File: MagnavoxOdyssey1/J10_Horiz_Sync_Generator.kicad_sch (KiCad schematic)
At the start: 15 parts

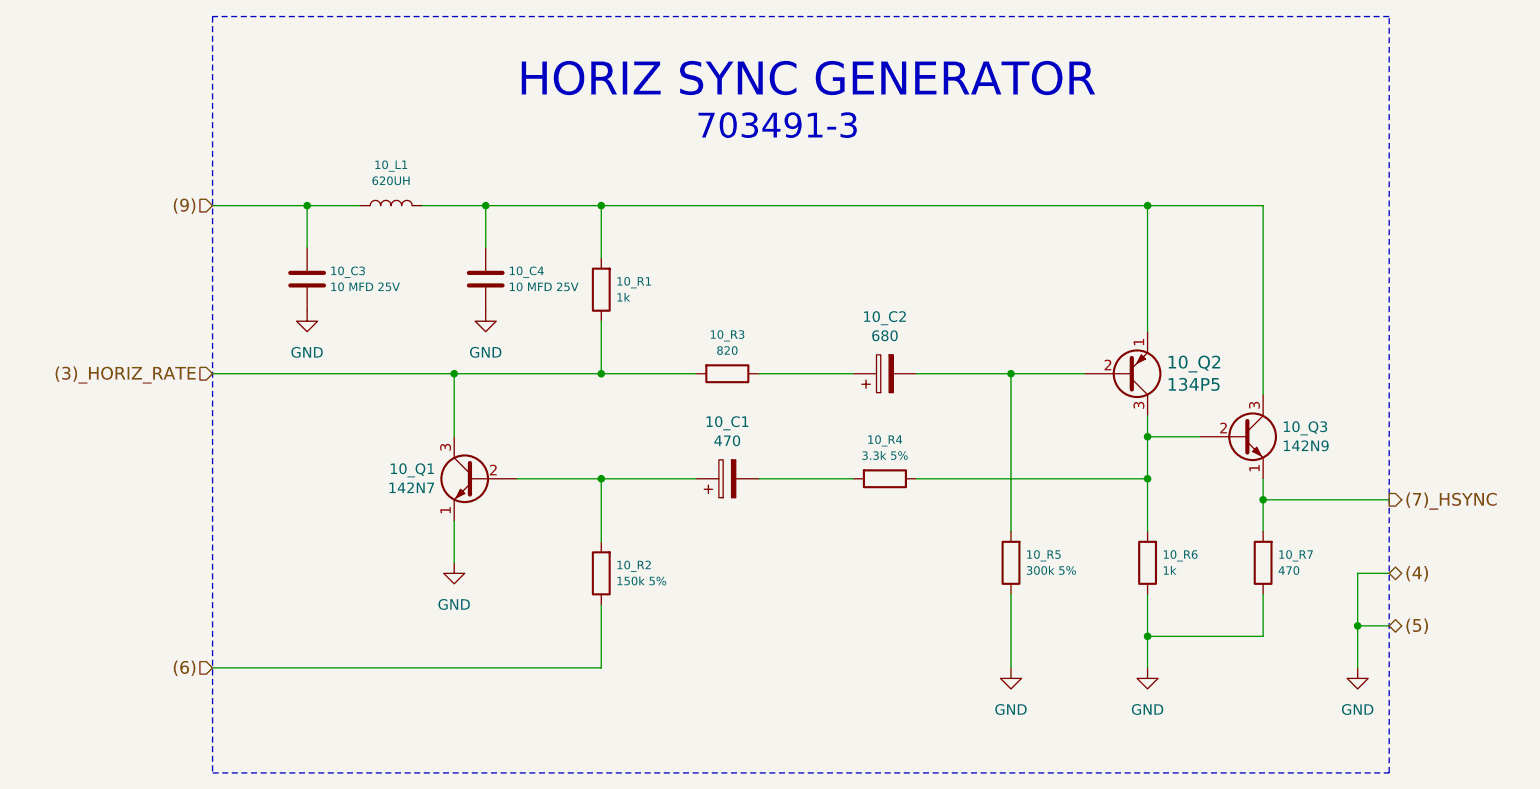
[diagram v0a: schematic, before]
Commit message: update to kicad 9
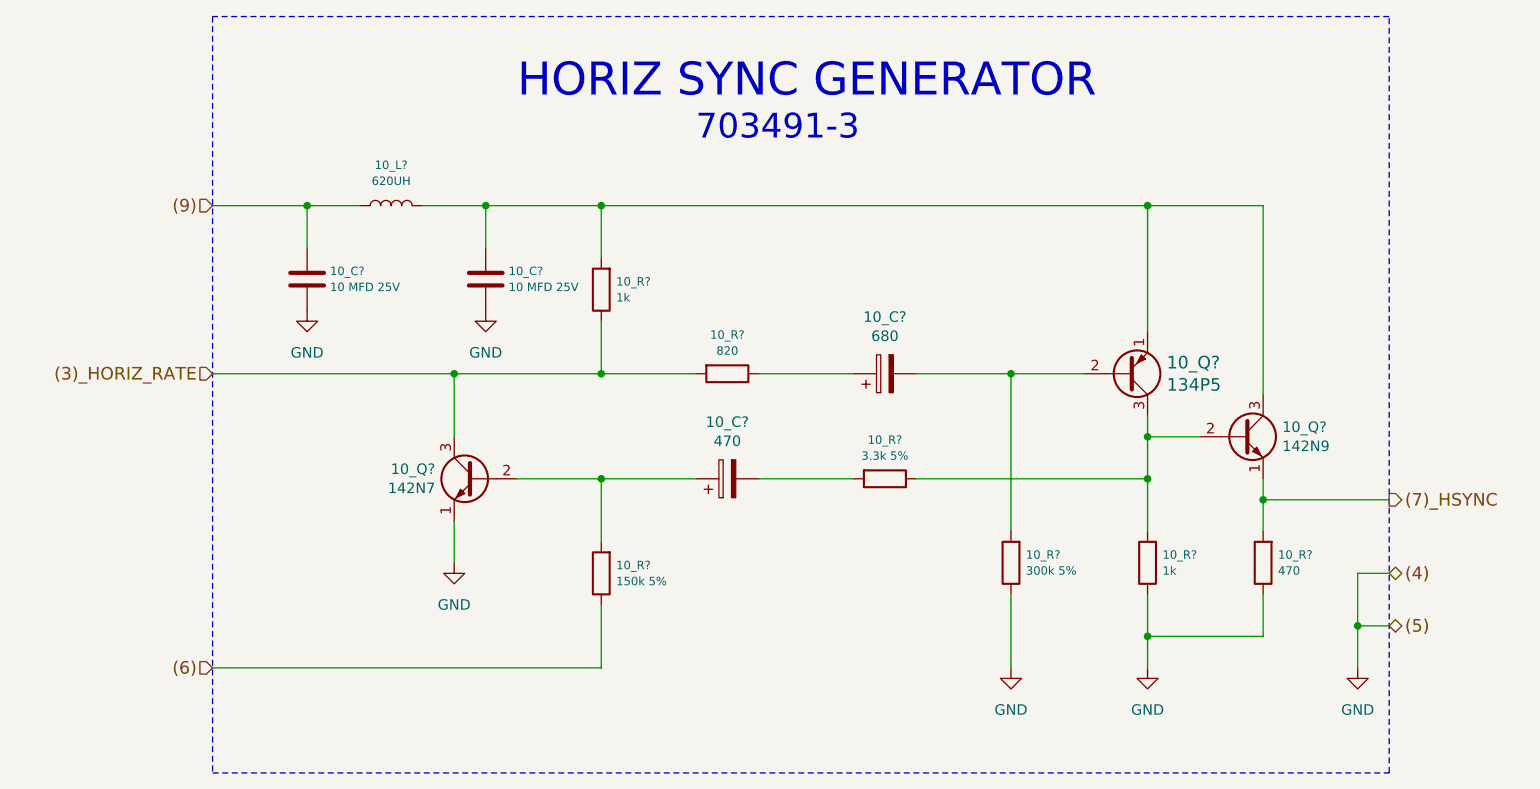
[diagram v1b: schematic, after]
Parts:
- 10_Q?: renamed from 10_Q1; symbol Device:Q_NPN_EBC -> Transistor_BJT:Q_NPN_EBC
- 10_Q?: renamed from 10_Q2; symbol Device:Q_PNP_EBC -> Transistor_BJT:Q_PNP_EBC
- 10_Q?: renamed from 10_Q3; symbol Device:Q_NPN_EBC -> Transistor_BJT:Q_NPN_EBC
- renumbered 10_C3 to 10_C?, 10_C4 to 10_C?, 10_C1 to 10_C?, 10_C2 to 10_C?, 10_L1 to 10_L?, 10_R1 to 10_R?, 10_R5 to 10_R?, 10_R6 to 10_R?, 10_R2 to 10_R?, 10_R7 to 10_R?, 10_R4 to 10_R?, 10_R3 to 10_R?
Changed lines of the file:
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@@
 (kicad_sch
-	(version 20231120)
+	(version 20250114)
 	(generator "eeschema")
-	(generator_version "8.0")
+	(generator_version "9.0")
 	(paper "A4")
+	(text "HORIZ SYNC GENERATOR"
+		(exclude_from_sim no)
+		(at 113.03 63.5 0)
+		(effects
+			(font
+				(size 3.9878 3.9878)
+			)
+			(justify left bottom)
+		)
+	)
+	(text "703491-3"
+		(exclude_from_sim no)
+		(at 134.62 68.58 0)
+		(effects
+			(font
+				(size 2.9972 2.9972)
+			)
+			(justify left bottom)
+		)
+	)
 	(junction
 		(at 123.19 76.2)
@@
 			(width 0)
 			(type default)
-		)
-	)
-	(text "HORIZ SYNC GENERATOR"
-		(exclude_from_sim no)
-		(at 113.03 63.5 0)
-		(effects
-			(font
-				(size 3.9878 3.9878)
-			)
-			(justify left bottom)
-		)
-	)
-	(text "703491-3"
-		(exclude_from_sim no)
-		(at 134.62 68.58 0)
-		(effects
-			(font
-				(size 2.9972 2.9972)
-			)
-			(justify left bottom)
 		)
 	)
@@
 		(on_board yes)
 		(dnp no)
-		(property "Reference" "10_C3"
+		(property "Reference" "10_C?"
 			(at 90.3986 84.1248 0)
 			(effects
@@
 		)
 		(pin "2"
+		)
+		(instances
+			(project "MagnavoxOdyssey1"
+				(path "/adb6e295-eae5-402e-a614-02a705c3e27c/00000000-0000-0000-0000-0000588f18cd"
+					(reference "10_C?")
+					(unit 1)
+				)
+			)
 		)
 	)
@@
 		(on_board yes)
 		(dnp no)
-		(property "Reference" "10_C4"
+		(property "Reference" "10_C?"
 			(at 111.9886 84.1248 0)
 			(effects
@@
 		)
 		(pin "2"
+		)
+		(instances
+			(project "MagnavoxOdyssey1"
+				(path "/adb6e295-eae5-402e-a614-02a705c3e27c/00000000-0000-0000-0000-0000588f18cd"
+					(reference "10_C?")
+					(unit 1)
+				)
+			)
 		)
 	)
@@
 		(on_board yes)
 		(dnp no)
-		(property "Reference" "10_L1"
+		(property "Reference" "10_L?"
 			(at 97.79 71.2978 90)
 			(effects
@@
 		)
 		(pin "2"
+		)
+		(instances
+			(project "MagnavoxOdyssey1"
+				(path "/adb6e295-eae5-402e-a614-02a705c3e27c/00000000-0000-0000-0000-0000588f18cd"
+					(reference "10_L?")
+					(unit 1)
+				)
+			)
 		)
 	)
@@
 		(on_board yes)
 		(dnp no)
-		(property "Reference" "10_R1"
+		(property "Reference" "10_R?"
 			(at 124.9934 85.3948 0)
 			(effects
@@
 		)
 		(pin "2"
+		)
+		(instances
+			(project "MagnavoxOdyssey1"
+				(path "/adb6e295-eae5-402e-a614-02a705c3e27c/00000000-0000-0000-0000-0000588f18cd"
+					(reference "10_R?")
+					(unit 1)
+				)
+			)
 		)
 	)
@@
 		(on_board yes)
 		(dnp no)
-		(property "Reference" "10_R5"
+		(property "Reference" "10_R?"
 			(at 174.5234 118.4148 0)
 			(effects
@@
 		)
 		(pin "2"
+		)
+		(instances
+			(project "MagnavoxOdyssey1"
+				(path "/adb6e295-eae5-402e-a614-02a705c3e27c/00000000-0000-0000-0000-0000588f18cd"
+					(reference "10_R?")
+					(unit 1)
+				)
+			)
 		)
 	)
@@
 		(on_board yes)
 		(dnp no)
-		(property "Reference" "10_R6"
+		(property "Reference" "10_R?"
 			(at 191.0334 118.4148 0)
 			(effects
@@
 		(pin "2"
 		)
+		(instances
+			(project "MagnavoxOdyssey1"
+				(path "/adb6e295-eae5-402e-a614-02a705c3e27c/00000000-0000-0000-0000-0000588f18cd"
+					(reference "10_R?")
+					(unit 1)
+				)
+			)
+		)
 	)
 	(symbol
-		(lib_id "Device:Q_NPN_EBC")
+		(lib_id "Transistor_BJT:Q_NPN_EBC")
 		(at 107.95 109.22 0)
 		(mirror y)
@@
 		(on_board yes)
 		(dnp no)
-		(property "Reference" "10_Q1"
+		(property "Reference" "10_Q?"
 			(at 103.124 108.0516 0)
 			(effects
@@
 		)
 		(pin "3"
+		)
+		(instances
+			(project "MagnavoxOdyssey1"
+				(path "/adb6e295-eae5-402e-a614-02a705c3e27c/00000000-0000-0000-0000-0000588f18cd"
+					(reference "10_Q?")
+					(unit 1)
+				)
+			)
 		)
 	)
@@
 		(on_board yes)
 		(dnp no)
-		(property "Reference" "10_R2"
+		(property "Reference" "10_R?"
 			(at 124.9934 119.6848 0)
 			(effects
@@
 		)
 		(pin "2"
+		)
+		(instances
+			(project "MagnavoxOdyssey1"
+				(path "/adb6e295-eae5-402e-a614-02a705c3e27c/00000000-0000-0000-0000-0000588f18cd"
+					(reference "10_R?")
+					(unit 1)
+				)
+			)
 		)
 	)
@@
 	)
 	(symbol
-		(lib_id "Device:Q_PNP_EBC")
+		(lib_id "Transistor_BJT:Q_PNP_EBC")
 		(at 186.69 96.52 0)
 		(mirror x)
@@
 		(on_board yes)
 		(dnp no)
-		(property "Reference" "10_Q2"
+		(property "Reference" "10_Q?"
 			(at 191.5414 95.1738 0)
 			(effects
@@
 		)
 		(pin "3"
+		)
+		(instances
+			(project "MagnavoxOdyssey1"
+				(path "/adb6e295-eae5-402e-a614-02a705c3e27c/00000000-0000-0000-0000-0000588f18cd"
+					(reference "10_Q?")
+					(unit 1)
+				)
+			)
 		)
 	)
@@
 	)
 	(symbol
-		(lib_id "Device:Q_NPN_EBC")
+		(lib_id "Transistor_BJT:Q_NPN_EBC")
 		(at 200.66 104.14 0)
 		(unit 1)
@@
 		(on_board yes)
 		(dnp no)
-		(property "Reference" "10_Q3"
+		(property "Reference" "10_Q?"
 			(at 205.5114 102.9716 0)
 			(effects
@@
 		)
 		(pin "3"
+		)
+		(instances
+			(project "MagnavoxOdyssey1"
+				(path "/adb6e295-eae5-402e-a614-02a705c3e27c/00000000-0000-0000-0000-0000588f18cd"
+					(reference "10_Q?")
+					(unit 1)
+				)
+			)
 		)
 	)
@@
 		(on_board yes)
 		(dnp no)
-		(property "Reference" "10_R7"
+		(property "Reference" "10_R?"
 			(at 205.0034 118.4148 0)
 			(effects
@@
 		)
 		(pin "2"
+		)
+		(instances
+			(project "MagnavoxOdyssey1"
+				(path "/adb6e295-eae5-402e-a614-02a705c3e27c/00000000-0000-0000-0000-0000588f18cd"
+					(reference "10_R?")
+					(unit 1)
+				)
+			)
 		)
 	)
@@
 		(on_board yes)
 		(dnp no)
-		(property "Reference" "10_R4"
+		(property "Reference" "10_R?"
 			(at 157.48 104.521 90)
 			(effects
@@
 		)
 		(pin "2"
+		)
+		(instances
+			(project "MagnavoxOdyssey1"
+				(path "/adb6e295-eae5-402e-a614-02a705c3e27c/00000000-0000-0000-0000-0000588f18cd"
+					(reference "10_R?")
+					(unit 1)
+				)
+			)
 		)
 	)
@@
 		(on_board yes)
 		(dnp no)
-		(property "Reference" "10_C1"
+		(property "Reference" "10_C?"
 			(at 138.43 102.362 90)
 			(effects
@@
 		)
 		(pin "2"
+		)
+		(instances
+			(project "MagnavoxOdyssey1"
+				(path "/adb6e295-eae5-402e-a614-02a705c3e27c/00000000-0000-0000-0000-0000588f18cd"
+					(reference "10_C?")
+					(unit 1)
+				)
+			)
 		)
 	)
@@
 		(on_board yes)
 		(dnp no)
-		(property "Reference" "10_C2"
+		(property "Reference" "10_C?"
 			(at 157.48 89.662 90)
 			(effects
@@
 		)
 		(pin "2"
+		)
+		(instances
+			(project "MagnavoxOdyssey1"
+				(path "/adb6e295-eae5-402e-a614-02a705c3e27c/00000000-0000-0000-0000-0000588f18cd"
+					(reference "10_C?")
+					(unit 1)
+				)
+			)
 		)
 	)
@@
 		(on_board yes)
 		(dnp no)
-		(property "Reference" "10_R3"
+		(property "Reference" "10_R?"
 			(at 138.43 91.821 90)
 			(effects
@@
 		(pin "2"
 		)
-	)
+		(instances
+			(project "MagnavoxOdyssey1"
+				(path "/adb6e295-eae5-402e-a614-02a705c3e27c/00000000-0000-0000-0000-0000588f18cd"
+					(reference "10_R?")
+					(unit 1)
+				)
+			)
+		)
+	)

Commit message: annotate
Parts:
- gave numbers to parts that had none: 15
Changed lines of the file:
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@@
 		(on_board yes)
 		(dnp no)
-		(property "Reference" "10_C?"
+		(property "Reference" "10_C1"
 			(at 90.3986 84.1248 0)
 			(effects
@@
 			(project "MagnavoxOdyssey1"
 				(path "/adb6e295-eae5-402e-a614-02a705c3e27c/00000000-0000-0000-0000-0000588f18cd"
-					(reference "10_C?")
+					(reference "10_C1")
 					(unit 1)
 				)
@@
 		(on_board yes)
 		(dnp no)
-		(property "Reference" "10_C?"
+		(property "Reference" "10_C2"
 			(at 111.9886 84.1248 0)
 			(effects
@@
 			(project "MagnavoxOdyssey1"
 				(path "/adb6e295-eae5-402e-a614-02a705c3e27c/00000000-0000-0000-0000-0000588f18cd"
-					(reference "10_C?")
+					(reference "10_C2")
 					(unit 1)
 				)
@@
 		(on_board yes)
 		(dnp no)
-		(property "Reference" "10_L?"
+		(property "Reference" "10_L1"
 			(at 97.79 71.2978 90)
 			(effects
@@
 			(project "MagnavoxOdyssey1"
 				(path "/adb6e295-eae5-402e-a614-02a705c3e27c/00000000-0000-0000-0000-0000588f18cd"
-					(reference "10_L?")
+					(reference "10_L1")
 					(unit 1)
 				)
@@
 		(on_board yes)
 		(dnp no)
-		(property "Reference" "10_R?"
+		(property "Reference" "10_R1"
 			(at 124.9934 85.3948 0)
 			(effects
@@
 			(project "MagnavoxOdyssey1"
 				(path "/adb6e295-eae5-402e-a614-02a705c3e27c/00000000-0000-0000-0000-0000588f18cd"
-					(reference "10_R?")
+					(reference "10_R1")
 					(unit 1)
 				)
@@
 		(on_board yes)
 		(dnp no)
-		(property "Reference" "10_R?"
+		(property "Reference" "10_R4"
 			(at 174.5234 118.4148 0)
 			(effects
@@
 			(project "MagnavoxOdyssey1"
 				(path "/adb6e295-eae5-402e-a614-02a705c3e27c/00000000-0000-0000-0000-0000588f18cd"
-					(reference "10_R?")
+					(reference "10_R4")
 					(unit 1)
 				)
@@
 		(on_board yes)
 		(dnp no)
-		(property "Reference" "10_R?"
+		(property "Reference" "10_R5"
 			(at 191.0334 118.4148 0)
 			(effects
@@
 			(project "MagnavoxOdyssey1"
 				(path "/adb6e295-eae5-402e-a614-02a705c3e27c/00000000-0000-0000-0000-0000588f18cd"
-					(reference "10_R?")
+					(reference "10_R5")
 					(unit 1)
 				)
@@
 		(on_board yes)
 		(dnp no)
-		(property "Reference" "10_Q?"
+		(property "Reference" "10_Q3"
 			(at 103.124 108.0516 0)
 			(effects
@@
 			(project "MagnavoxOdyssey1"
 				(path "/adb6e295-eae5-402e-a614-02a705c3e27c/00000000-0000-0000-0000-0000588f18cd"
-					(reference "10_Q?")
+					(reference "10_Q3")
 					(unit 1)
 				)
@@
 		(on_board yes)
 		(dnp no)
-		(property "Reference" "10_R?"
+		(property "Reference" "10_R7"
 			(at 124.9934 119.6848 0)
 			(effects
@@
 			(project "MagnavoxOdyssey1"
 				(path "/adb6e295-eae5-402e-a614-02a705c3e27c/00000000-0000-0000-0000-0000588f18cd"
-					(reference "10_R?")
+					(reference "10_R7")
 					(unit 1)
 				)
@@
 		(on_board yes)
 		(dnp no)
-		(property "Reference" "10_Q?"
+		(property "Reference" "10_Q1"
 			(at 191.5414 95.1738 0)
 			(effects
@@
 			(project "MagnavoxOdyssey1"
 				(path "/adb6e295-eae5-402e-a614-02a705c3e27c/00000000-0000-0000-0000-0000588f18cd"
-					(reference "10_Q?")
+					(reference "10_Q1")
 					(unit 1)
 				)
@@
 		(on_board yes)
 		(dnp no)
-		(property "Reference" "10_Q?"
+		(property "Reference" "10_Q2"
 			(at 205.5114 102.9716 0)
 			(effects
@@
 			(project "MagnavoxOdyssey1"
 				(path "/adb6e295-eae5-402e-a614-02a705c3e27c/00000000-0000-0000-0000-0000588f18cd"
-					(reference "10_Q?")
+					(reference "10_Q2")
 					(unit 1)
 				)
@@
 		(on_board yes)
 		(dnp no)
-		(property "Reference" "10_R?"
+		(property "Reference" "10_R6"
 			(at 205.0034 118.4148 0)
 			(effects
@@
 			(project "MagnavoxOdyssey1"
 				(path "/adb6e295-eae5-402e-a614-02a705c3e27c/00000000-0000-0000-0000-0000588f18cd"
-					(reference "10_R?")
+					(reference "10_R6")
 					(unit 1)
 				)
@@
 		(on_board yes)
 		(dnp no)
-		(property "Reference" "10_R?"
+		(property "Reference" "10_R3"
 			(at 157.48 104.521 90)
 			(effects
@@
 			(project "MagnavoxOdyssey1"
 				(path "/adb6e295-eae5-402e-a614-02a705c3e27c/00000000-0000-0000-0000-0000588f18cd"
-					(reference "10_R?")
+					(reference "10_R3")
 					(unit 1)
 				)
@@
 		(on_board yes)
 		(dnp no)
-		(property "Reference" "10_C?"
+		(property "Reference" "10_C4"
 			(at 138.43 102.362 90)
 			(effects
@@
 			(project "MagnavoxOdyssey1"
 				(path "/adb6e295-eae5-402e-a614-02a705c3e27c/00000000-0000-0000-0000-0000588f18cd"
-					(reference "10_C?")
+					(reference "10_C4")
 					(unit 1)
 				)
@@
 		(on_board yes)
 		(dnp no)
-		(property "Reference" "10_C?"
+		(property "Reference" "10_C3"
 			(at 157.48 89.662 90)
 			(effects
@@
 			(project "MagnavoxOdyssey1"
 				(path "/adb6e295-eae5-402e-a614-02a705c3e27c/00000000-0000-0000-0000-0000588f18cd"
-					(reference "10_C?")
+					(reference "10_C3")
 					(unit 1)
 				)
@@
 		(on_board yes)
 		(dnp no)
-		(property "Reference" "10_R?"
+		(property "Reference" "10_R2"
 			(at 138.43 91.821 90)
 			(effects
@@
 			(project "MagnavoxOdyssey1"
 				(path "/adb6e295-eae5-402e-a614-02a705c3e27c/00000000-0000-0000-0000-0000588f18cd"
-					(reference "10_R?")
-					(unit 1)
-				)
+					(reference "10_R2")
+					(unit 1)
+				)

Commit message: accurate resistors
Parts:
- 10_R3: value 3.3k 5% -> 3.3k
- 10_R4: value 300k 5% -> 300k
- 10_R7: value 150k 5% -> 150k
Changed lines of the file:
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@@
 			)
 		)
-		(property "Value" "300k 5%"
+		(property "Value" "300k"
 			(at 174.5234 120.3452 0)
 			(effects
@@
 			)
 		)
-		(property "Value" "150k 5%"
+		(property "Value" "150k"
 			(at 124.9934 121.6152 0)
 			(effects
@@
 			)
 		)
-		(property "Value" "3.3k 5%"
+		(property "Value" "3.3k"
 			(at 157.48 106.4514 90)
 			(effects
